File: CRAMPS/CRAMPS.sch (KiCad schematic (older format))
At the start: 13 parts, among them M101 LOGO_OSHW, M102 PCB_GREEN_RMC, P102 RESET, P106 CONN_3X2, Q101 2N7002, SW101 RESET

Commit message: Work in progress, many schematic updates, added PCB files
Signed-off-by: Charles Steinkuehler <charles@steinkuehler.net>
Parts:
- removed U? (x5): BEAGLEBONE, symbol BEAGLEBONE
- added P?: SERIAL0, symbol CONN_6
- added P?: POWER, symbol CONN_2
- added SW?: RESET, symbol SW_PUSH
- added U4: BEAGLEBONEBLACK, ~, symbol BEAGLEBONEBLACK
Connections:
- net labels added: /MACHINE_PWR, /RESET, AXIS_ENA, D3.3V, EMMC_ENA, ESTOP, MACHINE_PWR, PWR_BUT, SPI_CS0, SYS_5V, VDD_5V
- net labels removed: D13, E0_EN, ESTOP_OUT, IOREF, RESET, SPI_CS2, X_EN, Y_EN, Z_EN
- wire segments 34 -> 46
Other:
- note added: "24.576MHz"
- note added: "Audio"
- note removed: "Reset"
- note removed: "Serial header"
- moved on the sheet: D101, P102, Q101, R101, SW101

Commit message: Schematic updates mostly complete Pending pin assignment which will happen based on PCB layout Updated netlist imported to PCB, but placement not started
Signed-off-by: Charles Steinkuehler <charles@steinkuehler.net>
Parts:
- removed P106: CONN_3X2, symbol CONN_3X2
- SW102: renamed from SW?; value RESET -> POWER
- gave numbers to parts that had none: 2
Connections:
- net labels added: ADC_GND, ADC_VDD, AIN0, AIN1, AIN2, AIN3, DGND, FET4, FET5, FET6
- net labels removed: +3.3V, /MACHINE_PWR, A4, A5, A6, A7, AD14, AD15, AM-VIN, AREF, D10, D11-FET4, D12-FET5, D2-FET6, D23, D25, D27, D29, D31, D32, D33, D35, D37, D39, D41, D43, D45, D47, D49, D50-MISO, D51-MOSI, D52-SCK, D8, D9, DUE_5V, E1_EN, E2_EN, GNDA, PS-ON, SCL1, SDA1, THERM3, UART1_RX_LV, UART1_TX_LV, UART2_RX_LV, UART2_TX_LV, UART3_RX_LV, UART3_TX_LV
- wire segments 46 -> 23
- no-connect marks 2 -> 0
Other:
- note added: "BeagleBone\nserial header"
- note added: "Pull down"
- note added: "Pull up"
- note added: "SCL1 UART1_TX"
- note added: "SDA1 UART1_RX"
- note removed: "Limit switches connect via CBTD3861 to signals that would be\nuseful for GPMC interface (ale, ren, wen, wait0, etc). '3861 is\nenabled with a jumper in case GPMC device is used on the\nexpansion port."
- note removed: "Servo and secondary extruder signals connect to eMMC lines.\nServo uses '125 to isolate signals until enabled\nE1/E2 use enable pin to ignore step/dir"
- note removed: "The six existing axis enable signals are reduced to two:\nOne for XYZA (E0)\nOne for BC (E1 & E2)"

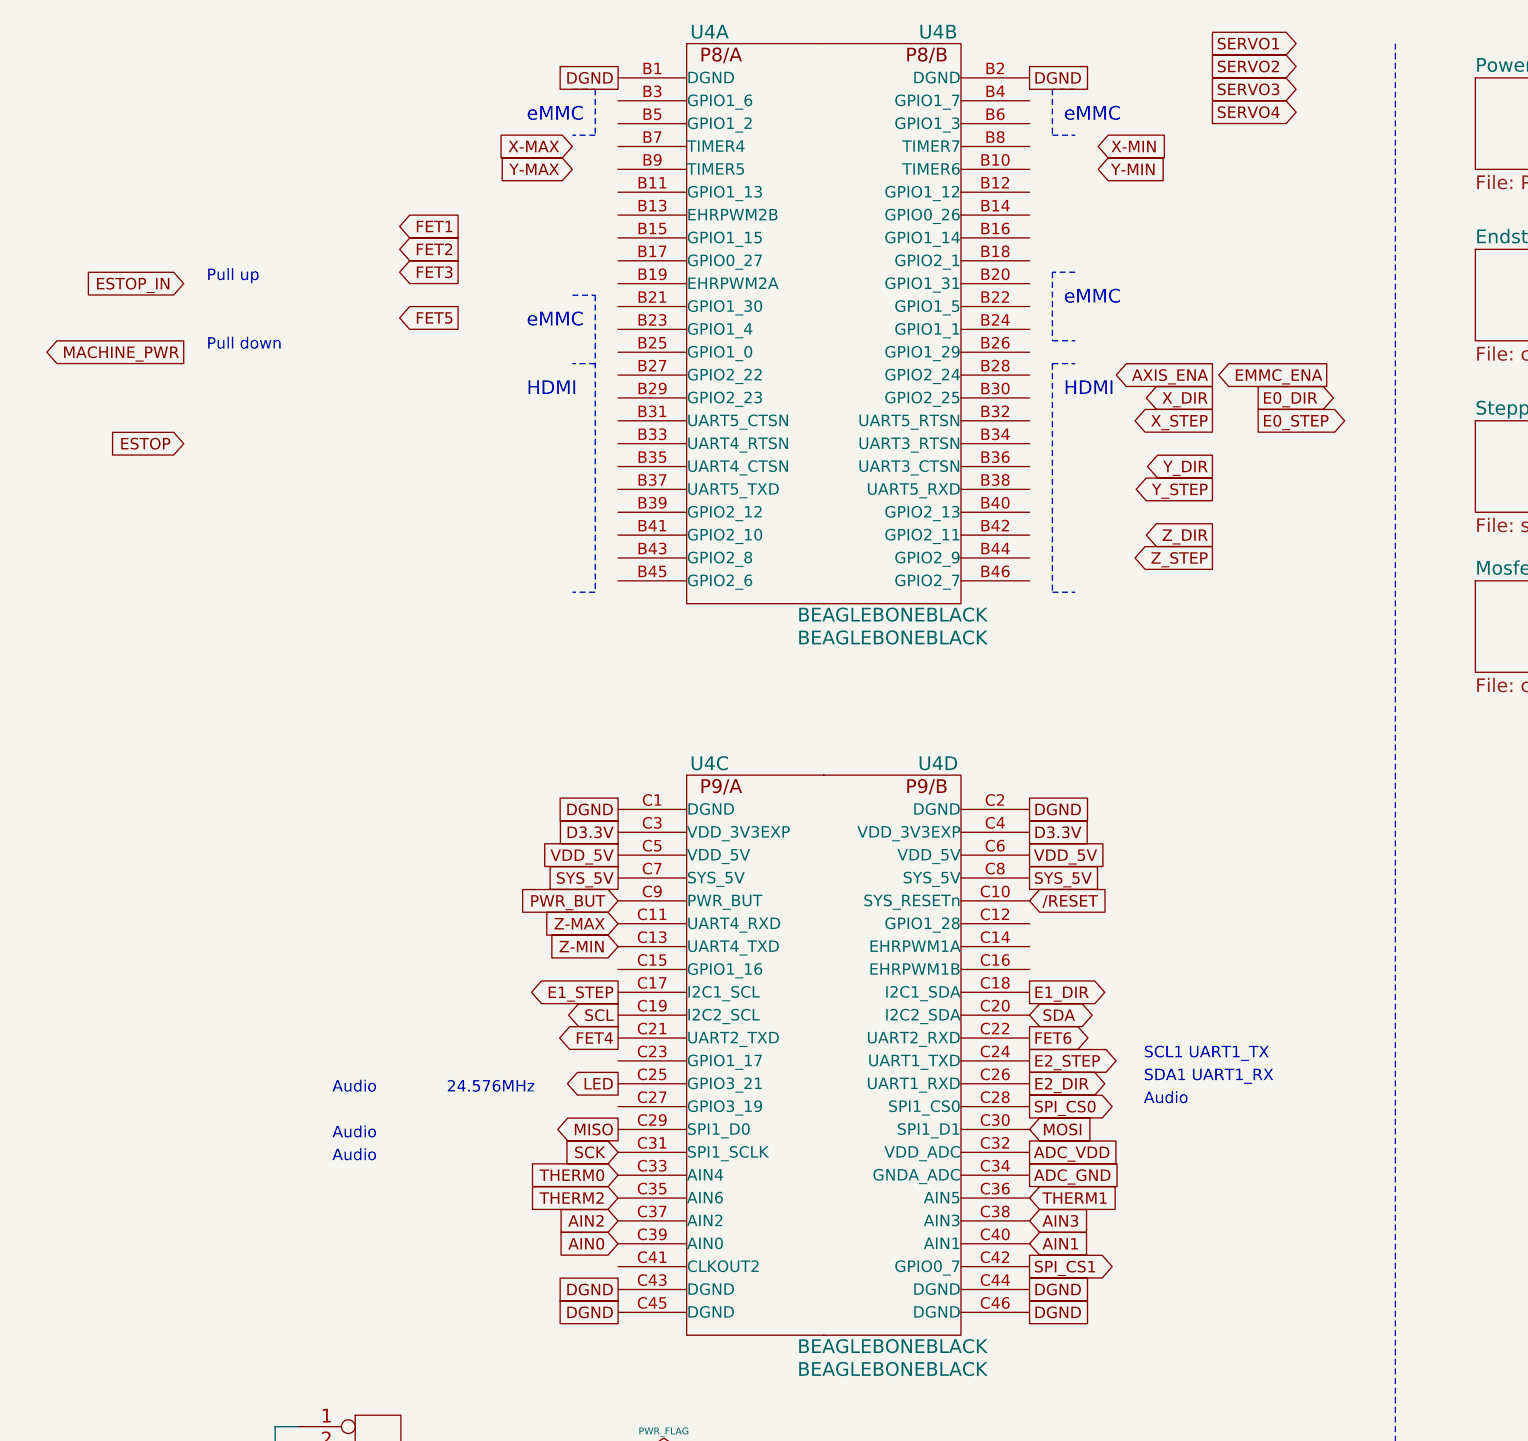
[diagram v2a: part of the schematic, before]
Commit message: P8/P9 Pins assigned, PCB placement in-progress
Signed-off-by: Charles Steinkuehler <charles@steinkuehler.net>
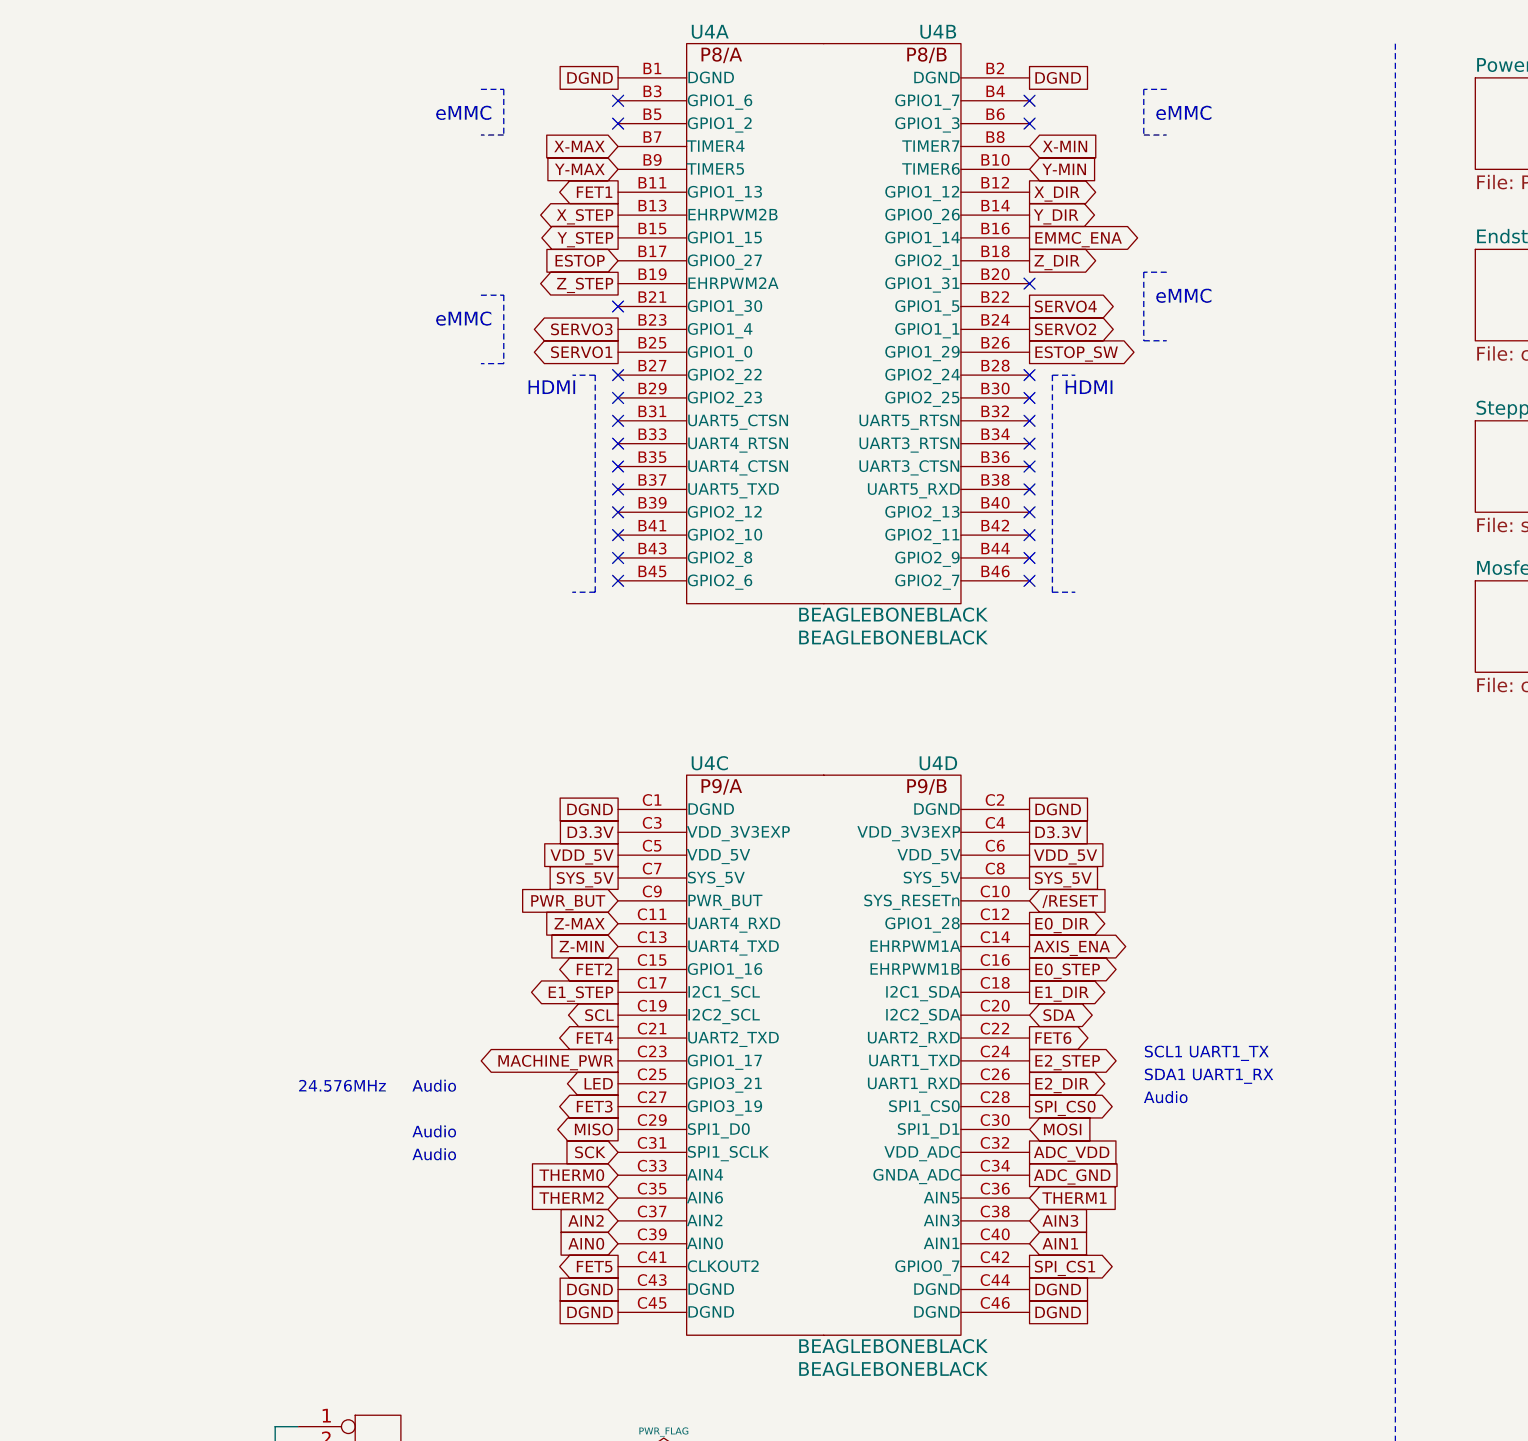
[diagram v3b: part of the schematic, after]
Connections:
- net AXIS_ENA: now also U4.C14 (EHRPWM1A)
- net E0_DIR: now also U4.C12 (GPIO1_28)
- net E0_STEP: now also U4.C16 (EHRPWM1B)
- net EMMC_ENA: now also U4.B16 (GPIO1_14)
- net ESTOP: now also U4.B17 (GPIO0_27)
- net FET1: now also U4.B11 (GPIO1_13)
- net FET2: now also U4.C15 (GPIO1_16)
- net FET3: now also U4.C27 (GPIO3_19)
- net FET5: now also U4.C41 (CLKOUT2)
- net MACHINE_PWR: now also U4.C23 (GPIO1_17)
- net SERVO1: now also U4.B25 (GPIO1_0)
- net SERVO2: now also U4.B24 (GPIO1_1)
- net SERVO3: now also U4.B23 (GPIO1_4)
- net SERVO4: now also U4.B22 (GPIO1_5)
- net X-MAX: now also U4.B7 (TIMER4)
- net X-MIN: now also U4.B8 (TIMER7)
- net X_DIR: now also U4.B12 (GPIO1_12)
- net X_STEP: now also U4.B13 (EHRPWM2B)
- net Y-MAX: now also U4.B9 (TIMER5)
- net Y-MIN: now also U4.B10 (TIMER6)
- net Y_DIR: now also U4.B14 (GPIO0_26)
- net Y_STEP: now also U4.B15 (GPIO1_15)
- net Z_DIR: now also U4.B18 (GPIO2_1)
- net Z_STEP: now also U4.B19 (EHRPWM2A)
- net ESTOP_SW: now reaches U4.B26 (GPIO1_29)
- no-connect marks 0 -> 26
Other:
- note removed: "Pull down"
- note removed: "Pull up"
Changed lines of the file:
@@
 Sheet 1 10
 Title "CRAMPS (Cape-RAMPS for BeagleBone)"
-Date "4 feb 2014"
+Date "6 feb 2014"
 Rev "v1.0"
 Comp ""
@@
 Text GLabel 3100 4500 0    50   Input ~ 0
 Z-MAX
-Text GLabel 2900 1200 0    50   Input ~ 0
+Text GLabel 3100 1200 0    50   Input ~ 0
 Y-MAX
-Text GLabel 5200 1200 2    50   Input ~ 0
+Text GLabel 4900 1200 2    50   Input ~ 0
 Y-MIN
-Text GLabel 5200 1100 2    50   Input ~ 0
+Text GLabel 4900 1100 2    50   Input ~ 0
 X-MIN
-Text GLabel 2900 1100 0    50   Input ~ 0
+Text GLabel 3100 1100 0    50   Input ~ 0
 X-MAX
-Text GLabel 5700 650  2    50   Output ~ 0
+Text GLabel 3100 2000 0    50   Output ~ 0
 SERVO1
-Text GLabel 5700 750  2    50   Output ~ 0
+Text GLabel 4900 1900 2    50   Output ~ 0
 SERVO2
-Text GLabel 5700 850  2    50   Output ~ 0
+Text GLabel 3100 1900 0    50   Output ~ 0
 SERVO3
-Text GLabel 5700 950  2    50   Output ~ 0
+Text GLabel 4900 1800 2    50   Output ~ 0
 SERVO4
 $Sheet
@@
 F1 "con_inputs.sch" 60
 $EndSheet
-Text GLabel 5700 2900 0    50   Output ~ 0
+Text GLabel 3100 1700 0    50   Output ~ 0
 Z_STEP
-Text GLabel 5700 2800 0    50   Output ~ 0
+Text GLabel 4900 1600 2    50   Output ~ 0
 Z_DIR
 Text GLabel 3100 4800 0    50   Output ~ 0
 E1_STEP
-Text GLabel 5700 2100 0    50   Output ~ 0
+Text GLabel 4900 4600 2    50   Output ~ 0
 AXIS_ENA
 Text GLabel 4900 4800 2    50   Output ~ 0
 E1_DIR
-Text GLabel 5900 2200 2    50   Output ~ 0
+Text GLabel 4900 4500 2    50   Output ~ 0
 E0_DIR
-Text GLabel 5900 2300 2    50   Output ~ 0
+Text GLabel 4900 4700 2    50   Output ~ 0
 E0_STEP
-Text GLabel 6200 2100 0    50   Output ~ 0
+Text GLabel 4900 1500 2    50   Output ~ 0
 EMMC_ENA
 Text GLabel 3100 5700 0    50   Input ~ 0
@@
 Text GLabel 3100 5600 0    50   Input ~ 0
 THERM0
-Text GLabel 5700 2500 0    50   Output ~ 0
+Text GLabel 4900 1400 2    50   Output ~ 0
 Y_DIR
-Text GLabel 5700 2600 0    50   Output ~ 0
+Text GLabel 3100 1500 0    50   Output ~ 0
 Y_STEP
-Text GLabel 5700 2200 0    50   Output ~ 0
+Text GLabel 4900 1300 2    50   Output ~ 0
 X_DIR
-Text GLabel 5700 2300 0    50   Output ~ 0
+Text GLabel 3100 1400 0    50   Output ~ 0
 X_STEP
 Text Notes 7700 6350 0    60   ~ 0
@@
 Text Notes 2700 2200 0    60   ~ 0
 HDMI
-Text Notes 5050 1000 0    60   ~ 0
+Text Notes 5450 1000 0    60   ~ 0
 eMMC
-Text Notes 5050 1800 0    60   ~ 0
+Text Notes 5450 1800 0    60   ~ 0
 eMMC
-Text Notes 2700 1000 0    60   ~ 0
+Text Notes 2300 1000 0    60   ~ 0
 eMMC
-Text Notes 2700 1900 0    60   ~ 0
+Text Notes 2300 1900 0    60   ~ 0
 eMMC
-Text GLabel 1200 2400 0    50   Input ~ 0
+Text GLabel 3100 1600 0    50   Input ~ 0
 ESTOP
-Text GLabel 1200 1700 0    50   Input ~ 0
-ESTOP_IN
+Text GLabel 4900 2000 2    50   Output ~ 0
+ESTOP_SW
 Text GLabel 4900 6000 2    50   Output ~ 0
 SPI_CS1
@@
 	-1   0    0    -1
 $EndComp
-Text GLabel 1200 2000 0    50   Output ~ 0
+Text GLabel 3100 5100 0    50   Output ~ 0
 MACHINE_PWR
-Text Notes 2350 5250 0    50   ~ 0
+Text Notes 1700 5250 0    50   ~ 0
 24.576MHz
-Text Notes 1850 5250 0    50   ~ 0
+Text Notes 2200 5250 0    50   ~ 0
 Audio
 Text Notes 5400 5300 0    50   ~ 0
 Audio
-Text Notes 1850 5450 0    50   ~ 0
+Text Notes 2200 5450 0    50   ~ 0
 Audio
-Text Notes 1850 5550 0    50   ~ 0
+Text Notes 2200 5550 0    50   ~ 0
 Audio
 $Comp
@@
 	7900 5400 7900 5200
 Wire Notes Line
-	5100 850  5000 850
-Wire Notes Line
-	5000 850  5000 1050
-Wire Notes Line
-	5000 1050 5100 1050
-Wire Notes Line
-	2900 850  3000 850
-Wire Notes Line
-	3000 850  3000 1050
-Wire Notes Line
-	3000 1050 2900 1050
-Wire Notes Line
-	5100 1650 5000 1650
-Wire Notes Line
-	5000 1650 5000 1950
-Wire Notes Line
-	5000 1950 5100 1950
-Wire Notes Line
-	2900 1750 3000 1750
-Wire Notes Line
-	3000 1750 3000 3050
+	5500 850  5400 850
+Wire Notes Line
+	5400 850  5400 1050
+Wire Notes Line
+	5400 1050 5500 1050
+Wire Notes Line
+	2500 850  2600 850
+Wire Notes Line
+	2600 850  2600 1050
+Wire Notes Line
+	2600 1050 2500 1050
+Wire Notes Line
+	5500 1650 5400 1650
+Wire Notes Line
+	5400 1650 5400 1950
+Wire Notes Line
+	5400 1950 5500 1950
+Wire Notes Line
+	2500 1750 2600 1750
+Wire Notes Line
+	3000 2100 3000 3050
 Wire Notes Line
 	5000 3050 5100 3050
@@
 	3000 3050 2900 3050
 Wire Notes Line
-	3000 2050 2900 2050
-Wire Notes Line
-	5000 2050 5000 3050
-Wire Notes Line
-	5000 2050 5100 2050
+	3000 2100 2900 2100
+Wire Notes Line
+	5000 2100 5000 3050
+Wire Notes Line
+	5000 2100 5100 2100
 Wire Wire Line
 	1700 6700 1600 6700
@@
 Text GLabel 3100 5000 0    50   Output ~ 0
 FET4
-Text GLabel 2400 1650 0    50   Output ~ 0
+Text GLabel 3100 5300 0    50   Output ~ 0
 FET3
-Text GLabel 2400 1550 0    50   Output ~ 0
+Text GLabel 3100 4700 0    50   Output ~ 0
 FET2
-Text GLabel 2400 1450 0    50   Output ~ 0
+Text GLabel 3100 1300 0    50   Output ~ 0
 FET1
-Text GLabel 2400 1850 0    50   Output ~ 0
+Text GLabel 3100 6000 0    50   Output ~ 0
 FET5
 Text GLabel 4900 5000 2    50   Output ~ 0
@@
 Text GLabel 4900 5600 2    50   UnSpc ~ 0
 ADC_GND
-Text Notes 1300 1700 0    50   ~ 0
-Pull up
-Text Notes 1300 2000 0    50   ~ 0
-Pull down
 Text Notes 1800 7400 0    50   ~ 0
 BeagleBone\nserial header
@@
 Text GLabel 3100 6900 0    50   UnSpc ~ 0
 DGND
+Wire Notes Line
+	2600 1750 2600 2050
+Wire Notes Line
+	2600 2050 2500 2050
+NoConn ~ 3100 900
+NoConn ~ 3100 1000
+NoConn ~ 3100 1800
+NoConn ~ 4900 900
+NoConn ~ 4900 1000
+NoConn ~ 4900 2100
+NoConn ~ 4900 2200
+NoConn ~ 4900 2300
+NoConn ~ 4900 2400
+NoConn ~ 4900 2500
+NoConn ~ 4900 2600
+NoConn ~ 4900 2700
+NoConn ~ 4900 2800
+NoConn ~ 4900 2900
+NoConn ~ 4900 3000
+NoConn ~ 3100 2100
+NoConn ~ 3100 2200
+NoConn ~ 3100 2300
+NoConn ~ 3100 2400
+NoConn ~ 3100 2500
+NoConn ~ 3100 2600
+NoConn ~ 3100 2700
+NoConn ~ 3100 2800
+NoConn ~ 3100 2900
+NoConn ~ 3100 3000
+NoConn ~ 4900 1700
 $EndSCHEMATC
